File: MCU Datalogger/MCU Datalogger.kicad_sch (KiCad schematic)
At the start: 25 parts, among them U1 24LC1025, U2 DS1337S_, U3 24LC1025, U4 ATMEGA328P-AU, Y1 32.768KHz, Y2 16MHz

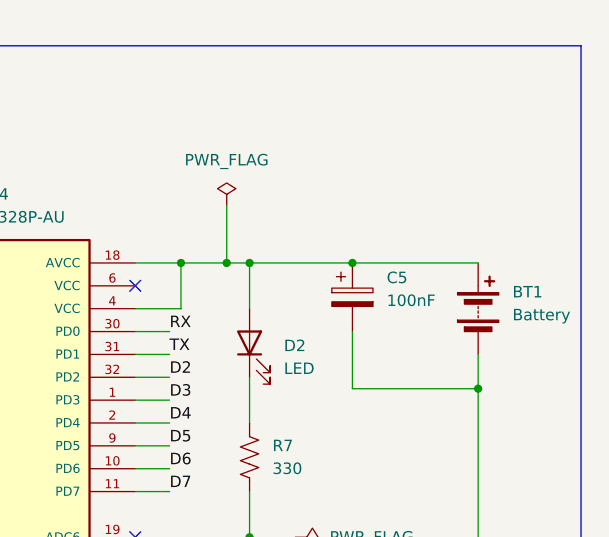
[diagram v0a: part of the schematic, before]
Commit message: 2layer: routing and silkscreen complete
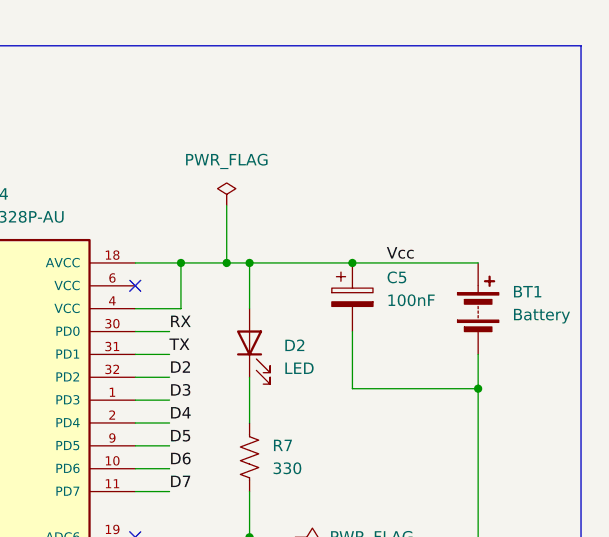
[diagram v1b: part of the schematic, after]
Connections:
- net Vcc: now also BT1.1 (+), C5.1, D2.2 (A), U4.18 (AVCC), U4.4 (VCC)
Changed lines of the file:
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@@
+		)
+	)
+	(label "Vcc"
+		(at 260.35 44.45 0)
+		(effects
+			(font
+				(size 1.27 1.27)
+			)
+			(justify left bottom)
 		)
 	)

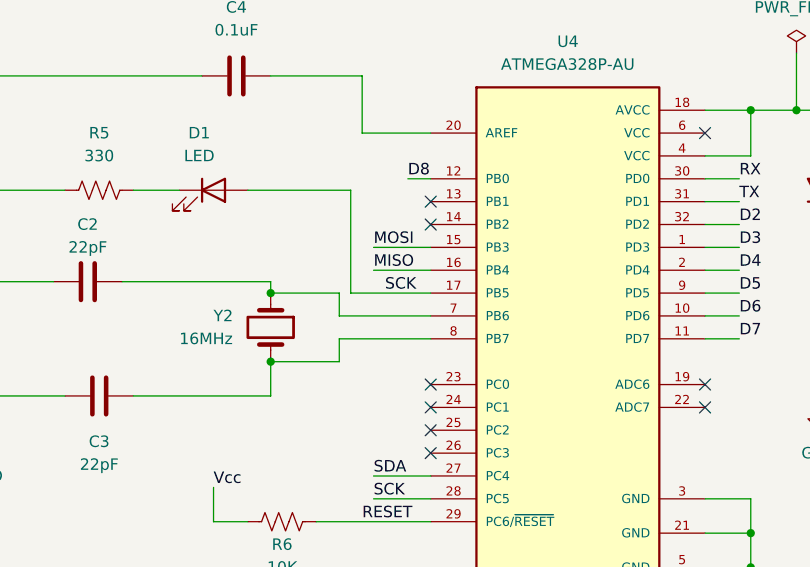
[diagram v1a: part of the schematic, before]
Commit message: 4layer: Completed 4layer routing of MCUdatalogger
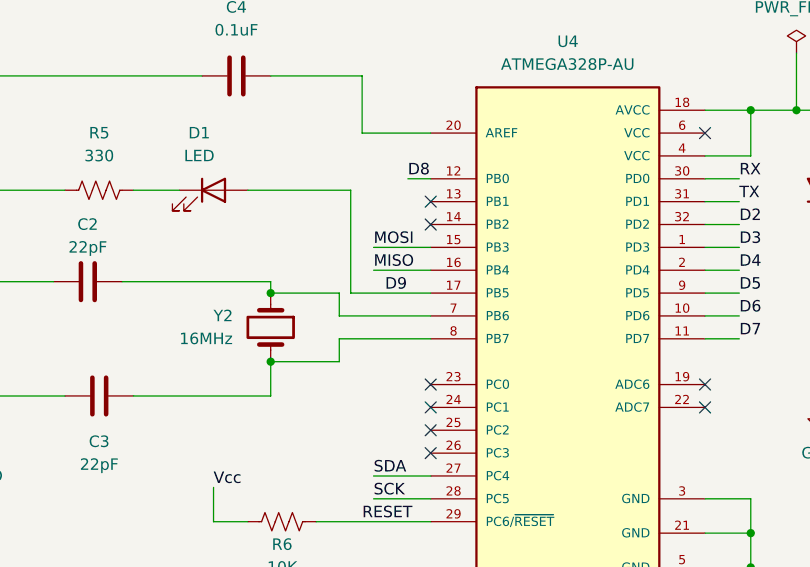
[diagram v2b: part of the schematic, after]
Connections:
- net SCK: no longer D1.2 (A), U4.17 (PB5)
- new net D9: D1.2 (A), U4.17 (PB5)
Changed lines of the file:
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@@
 		)
 	)
-	(label "SCK"
+	(label "D9"
 		(at 196.85 64.77 0)
 		(effects

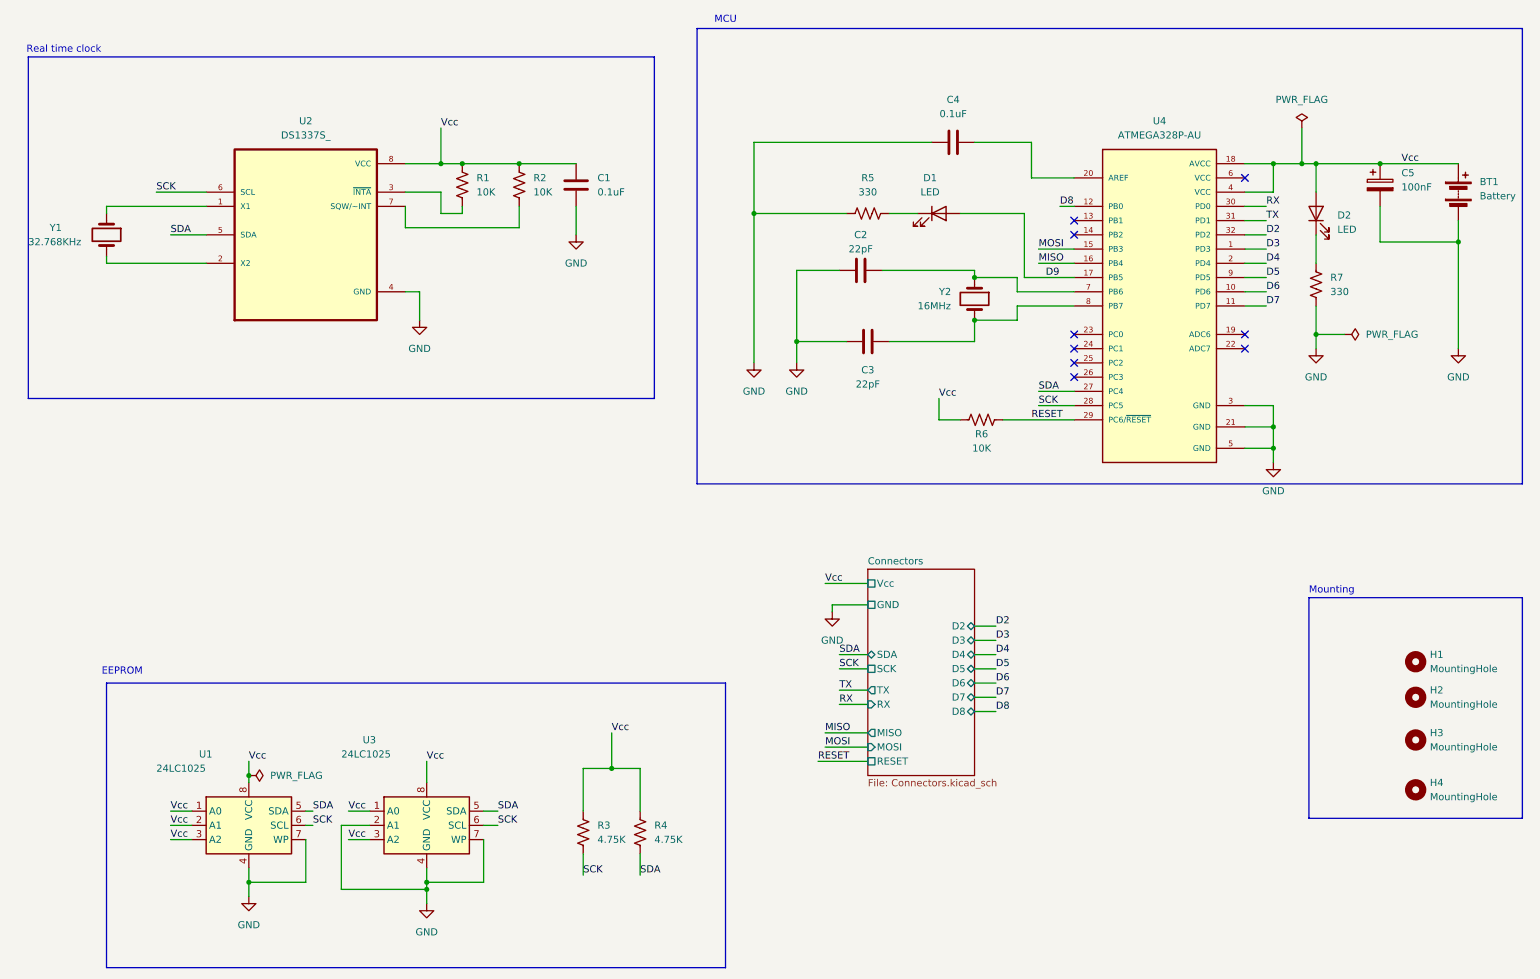
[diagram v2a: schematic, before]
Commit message: 4layer: recovered and corrected 4layer
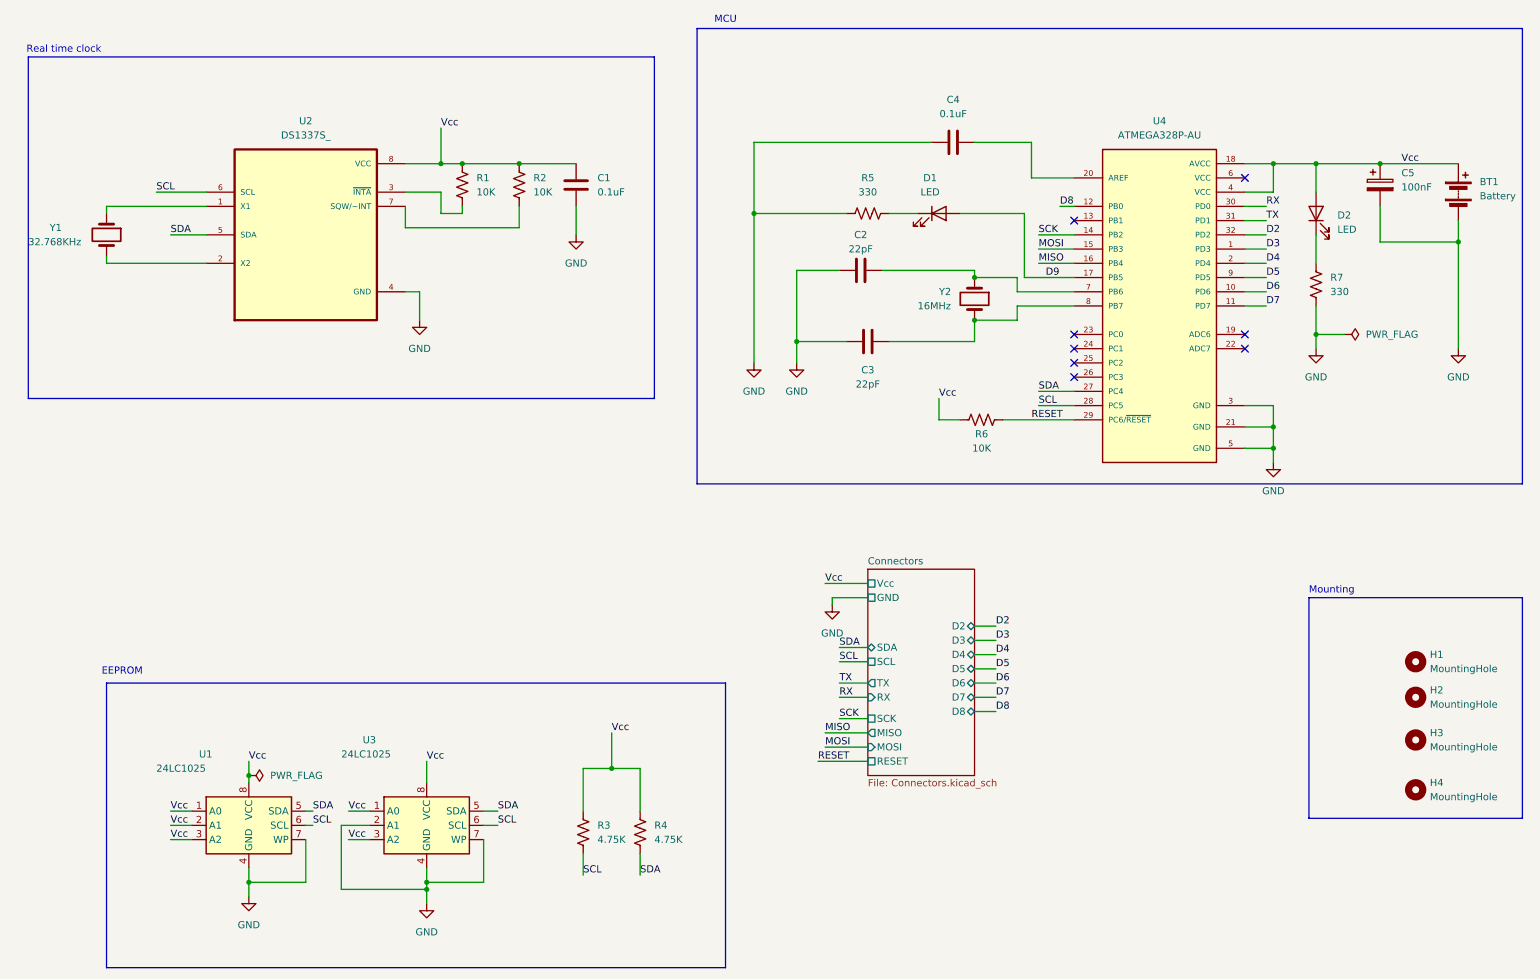
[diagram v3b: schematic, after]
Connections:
- net SCK: now also U4.14 (PB2); no longer R3.2, U1.6 (SCL), U2.6 (SCL), U3.6 (SCL), U4.28 (PC5)
- new net SCL: R3.2, U1.6 (SCL), U2.6 (SCL), U3.6 (SCL), U4.28 (PC5)
- no-connect marks 9 -> 8
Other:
- sheet Connectors ports: added SCL; removed none
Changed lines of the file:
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@@
 	)
 	(junction
-		(at 242.57 44.45)
-		(diameter 0)
-		(color 0 0 0 0)
-	)
-	(junction
 		(at 184.15 72.39)
 		(diameter 0)
@@
 	)
 	(no_connect
-		(at 201.93 57.15)
-	)
-	(no_connect
 		(at 232.41 46.99)
 	)
@@
 	(wire
 		(pts
-			(xy 86.36 173.99) (xy 86.36 176.53)
+			(xy 160.02 143.51) (xy 165.1 143.51)
 		)
 		(stroke
@@
 	(wire
 		(pts
-			(xy 184.15 132.08) (xy 187.96 132.08)
-		)
-		(stroke
-			(width 0)
-			(type default)
-		)
-	)
-	(wire
-		(pts
-			(xy 232.41 52.07) (xy 236.22 52.07)
+			(xy 86.36 173.99) (xy 86.36 176.53)
 		)
 		(stroke
@@
 	(wire
 		(pts
-			(xy 160.02 140.97) (xy 165.1 140.97)
+			(xy 184.15 132.08) (xy 187.96 132.08)
 		)
 		(stroke
@@
 	(wire
 		(pts
-			(xy 160.02 132.08) (xy 165.1 132.08)
+			(xy 232.41 52.07) (xy 236.22 52.07)
 		)
 		(stroke
@@
 	(wire
 		(pts
-			(xy 160.02 134.62) (xy 165.1 134.62)
-		)
-		(stroke
-			(width 0)
-			(type default)
-		)
-	)
-	(wire
-		(pts
 			(xy 184.15 40.64) (xy 194.31 40.64)
 		)
@@
 	(wire
 		(pts
-			(xy 237.49 44.45) (xy 242.57 44.45)
+			(xy 237.49 44.45) (xy 245.11 44.45)
 		)
 		(stroke
@@
 	(wire
 		(pts
+			(xy 160.02 139.7) (xy 165.1 139.7)
+		)
+		(stroke
+			(width 0)
+			(type default)
+		)
+	)
+	(wire
+		(pts
 			(xy 82.55 52.07) (xy 82.55 55.88)
 		)
@@
 	(wire
 		(pts
-			(xy 158.75 123.19) (xy 158.75 124.46)
+			(xy 158.75 121.92) (xy 158.75 123.19)
 		)
 		(stroke
@@
 	(wire
 		(pts
+			(xy 160.02 130.81) (xy 165.1 130.81)
+		)
+		(stroke
+			(width 0)
+			(type default)
+		)
+	)
+	(wire
+		(pts
 			(xy 54.61 151.13) (xy 54.61 153.67)
 		)
@@
 	(wire
 		(pts
-			(xy 242.57 38.1) (xy 242.57 44.45)
+			(xy 245.11 44.45) (xy 256.54 44.45)
 		)
 		(stroke
@@
 	(wire
 		(pts
-			(xy 245.11 44.45) (xy 256.54 44.45)
+			(xy 119.38 146.05) (xy 119.38 152.4)
 		)
 		(stroke
@@
 	(wire
 		(pts
-			(xy 119.38 146.05) (xy 119.38 152.4)
+			(xy 201.93 67.31) (xy 191.77 67.31)
 		)
 		(stroke
@@
 	(wire
 		(pts
-			(xy 201.93 67.31) (xy 191.77 67.31)
+			(xy 232.41 49.53) (xy 237.49 49.53)
 		)
 		(stroke
@@
 	(wire
 		(pts
-			(xy 232.41 49.53) (xy 237.49 49.53)
+			(xy 88.9 44.45) (xy 92.71 44.45)
 		)
 		(stroke
@@
 	(wire
 		(pts
-			(xy 88.9 44.45) (xy 92.71 44.45)
+			(xy 102.87 44.45) (xy 113.03 44.45)
 		)
 		(stroke
@@
 	(wire
 		(pts
-			(xy 102.87 44.45) (xy 113.03 44.45)
+			(xy 195.58 57.15) (xy 201.93 57.15)
 		)
 		(stroke
@@
 	(wire
 		(pts
+			(xy 160.02 133.35) (xy 165.1 133.35)
+		)
+		(stroke
+			(width 0)
+			(type default)
+		)
+	)
+	(wire
+		(pts
 			(xy 96.52 165.1) (xy 96.52 172.72)
 		)
@@
 	(wire
 		(pts
-			(xy 160.02 138.43) (xy 165.1 138.43)
-		)
-		(stroke
-			(width 0)
-			(type default)
-		)
-	)
-	(wire
-		(pts
 			(xy 184.15 76.2) (xy 184.15 72.39)
 		)
@@
 	(wire
 		(pts
-			(xy 157.48 146.05) (xy 165.1 146.05)
+			(xy 160.02 137.16) (xy 165.1 137.16)
 		)
 		(stroke
@@
 	(wire
 		(pts
-			(xy 232.41 67.31) (xy 236.22 67.31)
+			(xy 157.48 146.05) (xy 165.1 146.05)
 		)
 		(stroke
@@
 	(wire
 		(pts
-			(xy 242.57 44.45) (xy 245.11 44.45)
+			(xy 232.41 67.31) (xy 236.22 67.31)
 		)
 		(stroke
@@
 	(wire
 		(pts
-			(xy 165.1 123.19) (xy 158.75 123.19)
+			(xy 165.1 121.92) (xy 158.75 121.92)
 		)
 		(stroke
@@
 		)
 	)
-	(label "SCK"
+	(label "SCL"
 		(at 66.04 162.56 0)
 		(effects
@@
 		)
 	)
-	(label "SCK"
+	(label "SCL"
 		(at 38.1 49.53 0)
 		(effects
@@
 		)
 	)
+	(label "SCK"
+		(at 160.02 143.51 0)
+		(effects
+			(font
+				(size 1.27 1.27)
+			)
+			(justify left bottom)
+		)
+	)
 	(label "RX"
 		(at 236.22 52.07 0)
@@
 		)
 	)
-	(label "SCK"
-		(at 160.02 134.62 0)
+	(label "SCL"
+		(at 160.02 133.35 0)
 		(effects
 			(font
@@
 	)
 	(label "RX"
-		(at 160.02 140.97 0)
+		(at 160.02 139.7 0)
 		(effects
 			(font
@@
 		)
 	)
-	(label "SCK"
+	(label "SCL"
 		(at 99.06 162.56 0)
 		(effects
@@
 	)
 	(label "TX"
-		(at 160.02 138.43 0)
+		(at 160.02 137.16 0)
 		(effects
 			(font
@@
 	)
 	(label "SDA"
-		(at 160.02 132.08 0)
+		(at 160.02 130.81 0)
 		(effects
 			(font
@@
 		)
 	)
-	(label "SCK"
+	(label "SCL"
 		(at 114.3 171.45 0)
 		(effects
@@
 	)
 	(label "SCK"
+		(at 195.58 57.15 0)
+		(effects
+			(font
+				(size 1.27 1.27)
+			)
+			(justify left bottom)
+		)
+	)
+	(label "SCL"
 		(at 195.58 87.63 0)
 		(effects
@@
 	)
 	(symbol
-		(lib_id "power:PWR_FLAG")
-		(at 242.57 38.1 0)
-		(unit 1)
-		(exclude_from_sim no)
-		(in_bom yes)
-		(on_board yes)
-		(dnp no)
-		(fields_autoplaced yes)
-		(property "Reference" "#FLG02"
-			(at 242.57 36.195 0)
-			(effects
-				(font
-					(size 1.27 1.27)
-				)
-				(hide yes)
-			)
-		)
-		(property "Value" "PWR_FLAG"
-			(at 242.57 33.02 0)
-			(effects
-				(font
-					(size 1.27 1.27)
-				)
-			)
-		)
-		(property "Footprint" ""
-			(at 242.57 38.1 0)
-			(effects
-				(font
-					(size 1.27 1.27)
-				)
-				(hide yes)
-			)
-		)
-		(property "Datasheet" "~"
-			(at 242.57 38.1 0)
-			(effects
-				(font
-					(size 1.27 1.27)
-				)
-				(hide yes)
-			)
-		)
-		(property "Description" "Special symbol for telling ERC where power comes from"
-			(at 242.57 38.1 0)
-			(effects
-				(font
-					(size 1.27 1.27)
-				)
-				(hide yes)
-			)
-		)
-		(pin "1"
-		)
-		(instances
-			(project "MCU Datalogger"
-				(path "/1d19ab8e-eb81-412c-859a-e27f3101fb32"
-					(reference "#FLG02")
-					(unit 1)
-				)
-			)
-		)
-	)
-	(symbol
 		(lib_id "power:GND")
 		(at 245.11 77.47 0)
@@
 	(symbol
 		(lib_id "power:GND")
-		(at 158.75 124.46 0)
+		(at 158.75 123.19 0)
 		(unit 1)
 		(exclude_from_sim no)
@@
 		(fields_autoplaced yes)
 		(property "Reference" "#PWR010"
-			(at 158.75 130.81 0)
+			(at 158.75 129.54 0)
 			(effects
 				(font
@@
 		)
 		(property "Value" "GND"
-			(at 158.75 129.54 0)
+			(at 158.75 128.27 0)
 			(effects
 				(font
@@
 		)
 		(property "Footprint" ""
-			(at 158.75 124.46 0)
+			(at 158.75 123.19 0)
 			(effects
 				(font
@@
 		)
 		(property "Datasheet" ""
-			(at 158.75 124.46 0)
+			(at 158.75 123.19 0)
 			(effects
 				(font
@@
 		)
 		(property "Description" "Power symbol creates a global label with name \"GND\" , ground"
-			(at 158.75 124.46 0)
+			(at 158.75 123.19 0)
 			(effects
 				(font
@@
 		)
 		(pin "SDA" bidirectional
-			(at 165.1 132.08 180)
+			(at 165.1 130.81 180)
 			(effects
 				(font
@@
 		)
 		(pin "TX" output
-			(at 165.1 138.43 180)
+			(at 165.1 137.16 180)
 			(effects
 				(font
@@
 		)
 		(pin "RX" input
-			(at 165.1 140.97 180)
+			(at 165.1 139.7 180)
 			(effects
 				(font
@@
 		)
 		(pin "GND" passive
-			(at 165.1 123.19 180)
+			(at 165.1 121.92 180)
 			(effects
 				(font
@@
 			)
 		)
-		(pin "SCK" passive
-			(at 165.1 134.62 180)
+		(pin "SCL" passive
+			(at 165.1 133.35 180)
 			(effects
 				(font
@@
 			(effects
 				(font
+					(size 1.27 1.27)
+				)
+				(justify left)
+			)
+		)
+		(pin "SCK" passive
+			(at 165.1 143.51 180)
+			(effects
+				(font
